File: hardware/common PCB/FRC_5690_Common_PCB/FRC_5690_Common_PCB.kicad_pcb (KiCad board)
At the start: 2 copper layers, 74.8 x 76.6 mm, 37 parts, among them J1 5V in, J10 UART, J11 LED 0, J12 LED 1, J13 Analog In, J17 Conn_01x03_Pin, J18 Conn_01x03_Pin, J19 Conn_01x03_Pin, J2 I2C, J20 Conn_01x03_Pin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

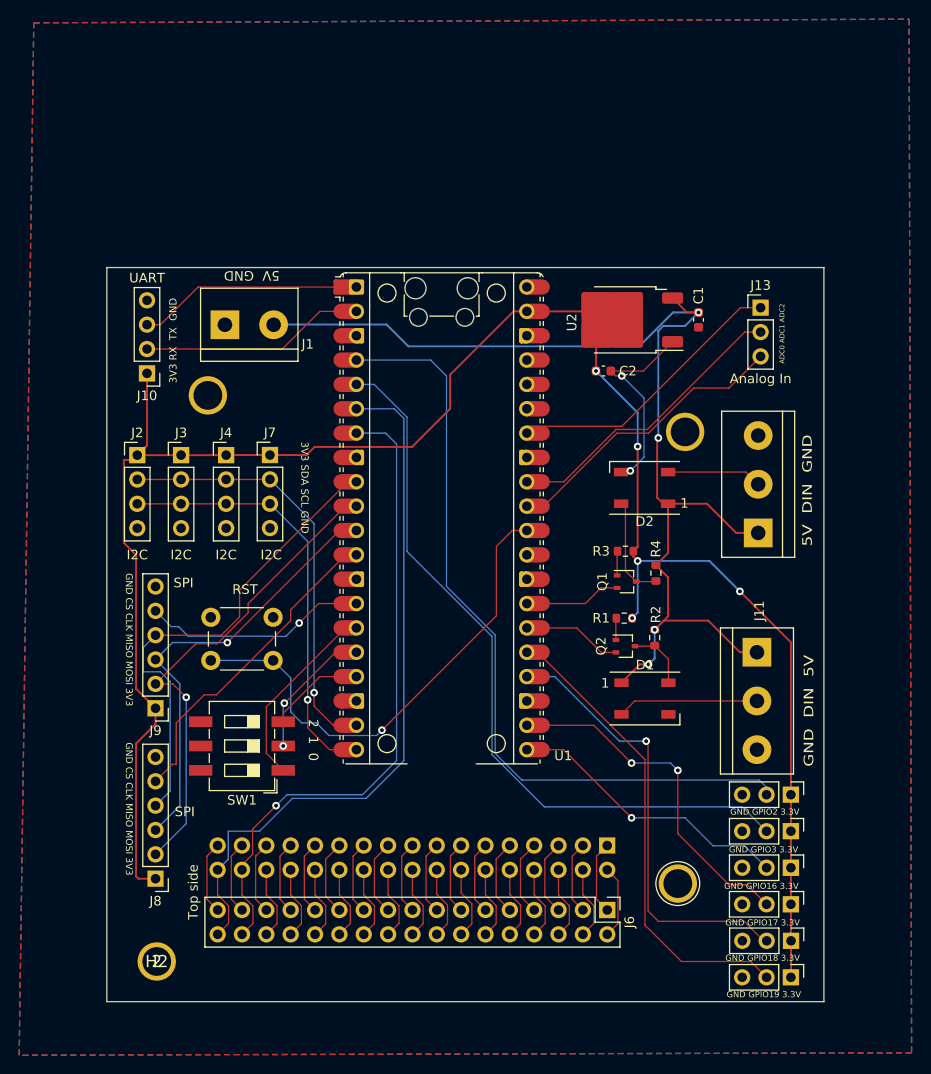
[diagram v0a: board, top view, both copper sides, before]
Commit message: migrate to Pico code and add micro SD card slot
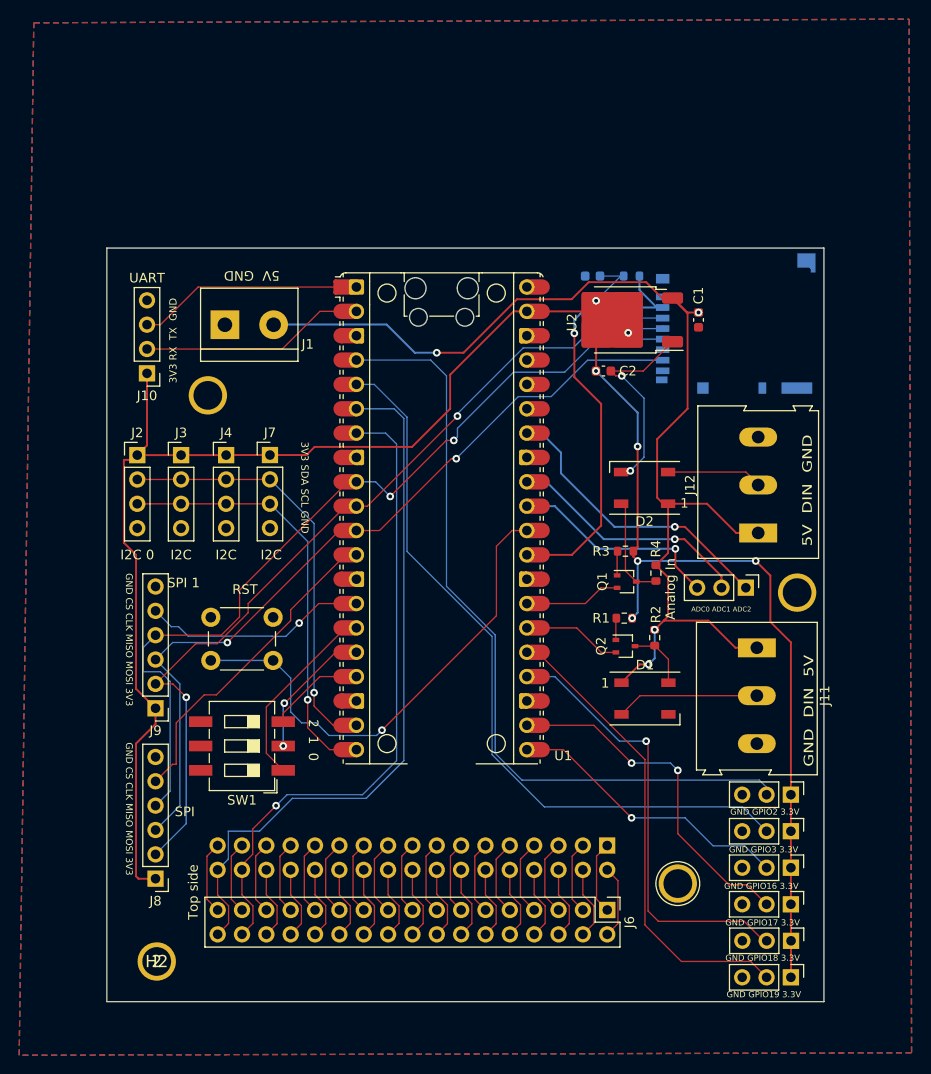
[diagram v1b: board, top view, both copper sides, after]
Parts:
- added C3: 100nF, Capacitor_SMD:C_0603_1608Metric, B.Cu at (149.9, 62.7)
- added J14: Micro_SD_Card, Connector_Card:microSD_HC_Hirose_DM3BT-DSF-PEJS, B.Cu at (164.8, 67.7)
- added R5: 1k, Resistor_SMD:R_0603_1608Metric, B.Cu at (153.9, 62.7)
- J11, J12: footprint TerminalBlock:TerminalBlock_bornier-3_P5.08mm -> TerminalBlock:TerminalBlock_Altech_AK300-3_P5.00mm
- J2: value I2C -> I2C 0
- J9: value SPI -> SPI 1
- moved J13 29.3 mm to (165.8, 95.2), turned to -90 degrees
- moved ? 20.4 mm to (171.2, 95.8)
- moved J11 0.47 mm to (167.0, 101.5)
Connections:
- U1 pad 29: unconnected-(U1-GPIO22-Pad29) -> /SD_CARD_CS
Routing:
- net /SD_CARD_CS: track 0.00 -> 46.0 mm, vias 0 -> 1
- net /SPI1_MOSI: track 50.7 -> 90.9 mm, vias 1 -> 2
- net /SPI1_CLK: track 50.4 -> 90.3 mm, vias 0 -> 2
- net /SPI1_MISO: track 46.4 -> 85.7 mm, vias 1 -> 2
- net +3.3V: track 201.2 -> 214.9 mm, vias 5 -> 7
- net /ADC0: track 30.9 -> 24.1 mm, vias 0 -> 1
- net /ADC1: track 30.9 -> 25.6 mm, vias 0 -> 1
- net /ADC2: track 29.8 -> 32.9 mm, vias 0 -> 1
- net +5V: track 117.9 -> 119.7 mm
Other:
- board size 74.8 x 76.6 mm -> 74.8 x 78.6 mm

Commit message: Add bottom silkscreen text to PCB
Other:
- board text added: "Designed by Evan Rust for FRC team 5690"
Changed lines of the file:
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@@
   (gr_rect (start 99.187 59.817) (end 173.99 138.43)
     (stroke (width 0.1) (type default)) (fill none) (layer "Edge.Cuts"))
+  (gr_text "Designed by Evan Rust for FRC team 5690" (at 151.003 117.094) (layer "B.SilkS")
+    (effects (font (size 1 1) (thickness 0.15)) (justify left bottom mirror))
+  )
   (gr_text "5V  GND" (at 117.221 62.103 180) (layer "F.SilkS")
     (effects (font (size 1 1) (thickness 0.15)) (justify left bottom))

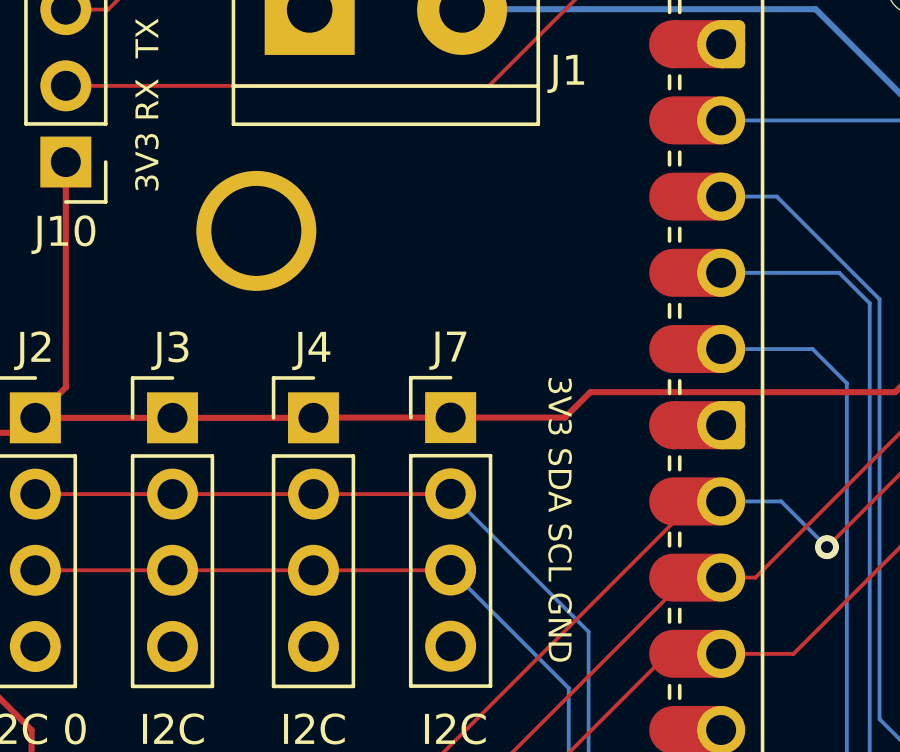
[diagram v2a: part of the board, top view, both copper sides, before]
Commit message: Add EEPROM
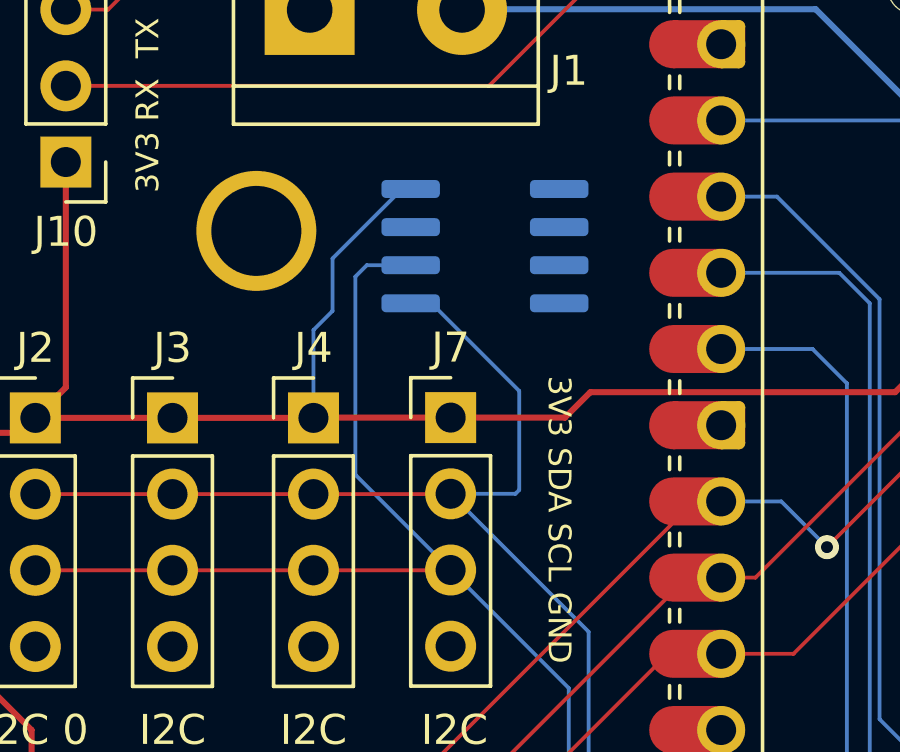
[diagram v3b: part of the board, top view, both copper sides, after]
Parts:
- added U3: AT24CS02-SSHM, Package_SO:SOIC-8_3.9x4.9mm_P1.27mm, B.Cu at (117.3, 75.7)
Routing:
- net /I2C1_SCL: track 44.9 -> 58.0 mm
- net /I2C1_SDA: track 44.6 -> 55.1 mm
- net +3.3V: track 214.9 -> 224.1 mm
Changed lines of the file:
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@@
+    )
+  )
+  (footprint "Package_SO:SOIC-8_3.9x4.9mm_P1.27mm" (layer "B.Cu")
+    (at 117.348 75.692 180)
+    (descr "SOIC, 8 Pin (JEDEC MS-012AA, https://www.analog.com/media/en/package-pcb-resources/package/pkg_pdf/soic_narrow-r/r_8.pdf), generated with kicad-footprint-generator ipc_gullwing_generator.py")
+    (tags "SOIC SO")
+    (property "Sheetfile" "FRC_5690_Common_PCB.kicad_sch")
+    (property "Sheetname" "")
+    (property "ki_description" "I2C Serial EEPROM, 2Kb (256x8) with Unique Serial Number, SO8")
+    (property "ki_keywords" "I2C Serial EEPROM Nonvolatile Memory")
+    (attr smd)
+    (fp_text reference "U3" (at 0 3.4) (layer "B.SilkS")
+        (effects (font (size 1 1) (thickness 0.15)) (justify mirror))
+    )
+    (fp_text value "AT24CS02-SSHM" (at 0 -3.4) (layer "B.Fab")
+        (effects (font (size 1 1) (thickness 0.15)) (justify mirror))
+    )
+    (fp_text user "${REFERENCE}" (at 0 0) (layer "B.Fab")
+        (effects (font (size 0.98 0.98) (thickness 0.15)) (justify mirror))
+    )
+    (fp_line (start 0 -2.56) (end -1.95 -2.56)
+      (stroke (width 0.12) (type solid)) (layer "B.SilkS"))
+    (fp_line (start 0 -2.56) (end 1.95 -2.56)
+      (stroke (width 0.12) (type solid)) (layer "B.SilkS"))
+    (fp_line (start 0 2.56) (end -3.45 2.56)
+      (stroke (width 0.12) (type solid)) (layer "B.SilkS"))
+    (fp_line (start 0 2.56) (end 1.95 2.56)
+      (stroke (width 0.12) (type solid)) (layer "B.SilkS"))
+    (fp_line (start -3.7 -2.7) (end 3.7 -2.7)
+      (stroke (width 0.05) (type solid)) (layer "B.CrtYd"))
+    (fp_line (start -3.7 2.7) (end -3.7 -2.7)
+      (stroke (width 0.05) (type solid)) (layer "B.CrtYd"))
+    (fp_line (start 3.7 -2.7) (end 3.7 2.7)
+      (stroke (width 0.05) (type solid)) (layer "B.CrtYd"))
+    (fp_line (start 3.7 2.7) (end -3.7 2.7)
+      (stroke (width 0.05) (type solid)) (layer "B.CrtYd"))
+    (fp_line (start -1.95 -2.45) (end -1.95 1.475)
+      (stroke (width 0.1) (type solid)) (layer "B.Fab"))
+    (fp_line (start -1.95 1.475) (end -0.975 2.45)
+      (stroke (width 0.1) (type solid)) (layer "B.Fab"))
+    (fp_line (start -0.975 2.45) (end 1.95 2.45)
+      (stroke (width 0.1) (type solid)) (layer "B.Fab"))
+    (fp_line (start 1.95 -2.45) (end -1.95 -2.45)
+      (stroke (width 0.1) (type solid)) (layer "B.Fab"))
+    (fp_line (start 1.95 2.45) (end 1.95 -2.45)
+      (stroke (width 0.1) (type solid)) (layer "B.Fab"))
+    (pad "1" smd roundrect (at -2.475 1.905 180) (size 1.95 0.6) (layers "B.Cu" "B.Paste" "B.Mask") (roundrect_rratio 0.25)
+      (net 7 "GND") (pinfunction "A0") (pintype "input"))
+    (pad "2" smd roundrect (at -2.475 0.635 180) (size 1.95 0.6) (layers "B.Cu" "B.Paste" "B.Mask") (roundrect_rratio 0.25)
+      (net 7 "GND") (pinfunction "A1") (pintype "input"))
+    (pad "3" smd roundrect (at -2.475 -0.635 180) (size 1.95 0.6) (layers "B.Cu" "B.Paste" "B.Mask") (roundrect_rratio 0.25)
+      (net 7 "GND") (pinfunction "A2") (pintype "input"))
+    (pad "4" smd roundrect (at -2.475 -1.905 180) (size 1.95 0.6) (layers "B.Cu" "B.Paste" "B.Mask") (roundrect_rratio 0.25)
+      (net 7 "GND") (pinfunction "GND") (pintype "power_in"))
+    (pad "5" smd roundrect (at 2.475 -1.905 180) (size 1.95 0.6) (layers "B.Cu" "B.Paste" "B.Mask") (roundrect_rratio 0.25)
+      (net 13 "/I2C1_SDA") (pinfunction "SDA") (pintype "bidirectional"))
+    (pad "6" smd roundrect (at 2.475 -0.635 180) (size 1.95 0.6) (layers "B.Cu" "B.Paste" "B.Mask") (roundrect_rratio 0.25)
+      (net 14 "/I2C1_SCL") (pinfunction "SCL") (pintype "input"))
+    (pad "7" smd roundrect (at 2.475 0.635 180) (size 1.95 0.6) (layers "B.Cu" "B.Paste" "B.Mask") (roundrect_rratio 0.25)
+      (net 7 "GND") (pinfunction "WP") (pintype "input"))
+    (pad "8" smd roundrect (at 2.475 1.905 180) (size 1.95 0.6) (layers "B.Cu" "B.Paste" "B.Mask") (roundrect_rratio 0.25)
+      (net 8 "+3.3V") (pinfunction "VCC") (pintype "power_in"))
+    (model "${KICAD6_3DMODEL_DIR}/Package_SO.3dshapes/SOIC-8_3.9x4.9mm_P1.27mm.wrl"
+      (offset (xyz 0 0 0))
+      (scale (xyz 1 1 1))
+      (rotate (xyz 0 0 0))
     )
   )
@@
   (via (at 154.559 92.456) (size 0.8) (drill 0.4) (layers "F.Cu" "B.Cu") (net 8))
   (via (at 154.559 80.518) (size 0.8) (drill 0.4) (layers "F.Cu" "B.Cu") (net 8))
+  (segment (start 114.583223 73.787) (end 112.268 76.102223) (width 0.127) (layer "B.Cu") (net 8))
+  (segment (start 114.873 73.787) (end 114.583223 73.787) (width 0.127) (layer "B.Cu") (net 8))
   (segment (start 154.559 97.853) (end 153.987 98.425) (width 0.2032) (layer "B.Cu") (net 8))
   (segment (start 150.635 62.738) (end 153.099 62.738) (width 0.127) (layer "B.Cu") (net 8))
   (segment (start 154.559 80.518) (end 154.559 76.988) (width 0.2032) (layer "B.Cu") (net 8))
+  (segment (start 112.268 76.102223) (end 112.268 77.851) (width 0.127) (layer "B.Cu") (net 8))
   (segment (start 154.559 92.456) (end 154.559 97.853) (width 0.2032) (layer "B.Cu") (net 8))
+  (segment (start 112.268 77.851) (end 111.633 78.486) (width 0.127) (layer "B.Cu") (net 8))
   (segment (start 157.169 68.219) (end 154.014 68.219) (width 0.127) (layer "B.Cu") (net 8))
+  (segment (start 111.633 78.486) (end 111.633 81.417) (width 0.127) (layer "B.Cu") (net 8))
   (segment (start 156.718 68.453) (end 157.226 67.945) (width 0.2032) (layer "B.Cu") (net 8))
   (segment (start 152.8069 62.738) (end 150.227 65.3179) (width 0.127) (layer "B.Cu") (net 8))
@@
   (segment (start 120.805 107.597) (end 120.805 106.196312) (width 0.127) (layer "F.Cu") (net 13))
   (via (at 120.805 106.196312) (size 0.8) (drill 0.4) (layers "F.Cu" "B.Cu") (net 13))
+  (segment (start 118.491 80.518) (end 118.491 83.82) (width 0.127) (layer "B.Cu") (net 13))
   (segment (start 120.805 106.196312) (end 120.805 88.547) (width 0.127) (layer "B.Cu") (net 13))
+  (segment (start 118.491 83.82) (end 118.364 83.947) (width 0.127) (layer "B.Cu") (net 13))
+  (segment (start 114.873 77.597) (end 115.57 77.597) (width 0.127) (layer "B.Cu") (net 13))
   (segment (start 120.805 88.547) (end 116.205 83.947) (width 0.127) (layer "B.Cu") (net 13))
+  (segment (start 118.364 83.947) (end 116.205 83.947) (width 0.127) (layer "B.Cu") (net 13))
+  (segment (start 115.57 77.597) (end 118.491 80.518) (width 0.127) (layer "B.Cu") (net 13))
   (segment (start 122.428 112.141) (end 125.222 112.141) (width 0.127) (layer "F.Cu") (net 14))
   (segment (start 106.934 86.497) (end 111.633 86.497) (width 0.127) (layer "F.Cu") (net 14))
@@
   (segment (start 120.142 106.934576) (end 120.142 90.424) (width 0.127) (layer "B.Cu") (net 14))
   (segment (start 120.13688 106.939696) (end 120.142 106.934576) (width 0.127) (layer "B.Cu") (net 14))
+  (segment (start 114.873 76.327) (end 113.411 76.327) (width 0.127) (layer "B.Cu") (net 14))
+  (segment (start 113.03 76.708) (end 113.03 83.312) (width 0.127) (layer "B.Cu") (net 14))
+  (segment (start 113.03 83.312) (end 116.205 86.487) (width 0.127) (layer "B.Cu") (net 14))
   (segment (start 120.142 90.424) (end 116.205 86.487) (width 0.127) (layer "B.Cu") (net 14))
+  (segment (start 113.411 76.327) (end 113.03 76.708) (width 0.127) (layer "B.Cu") (net 14))
   (segment (start 152.502499 130.293363) (end 151.388999 131.406863) (width 0.127) (layer "F.Cu") (net 15))
   (segment (start 152.502499 125.799361) (end 152.502499 130.293363) (width 0.127) (layer "F.Cu") (net 15))

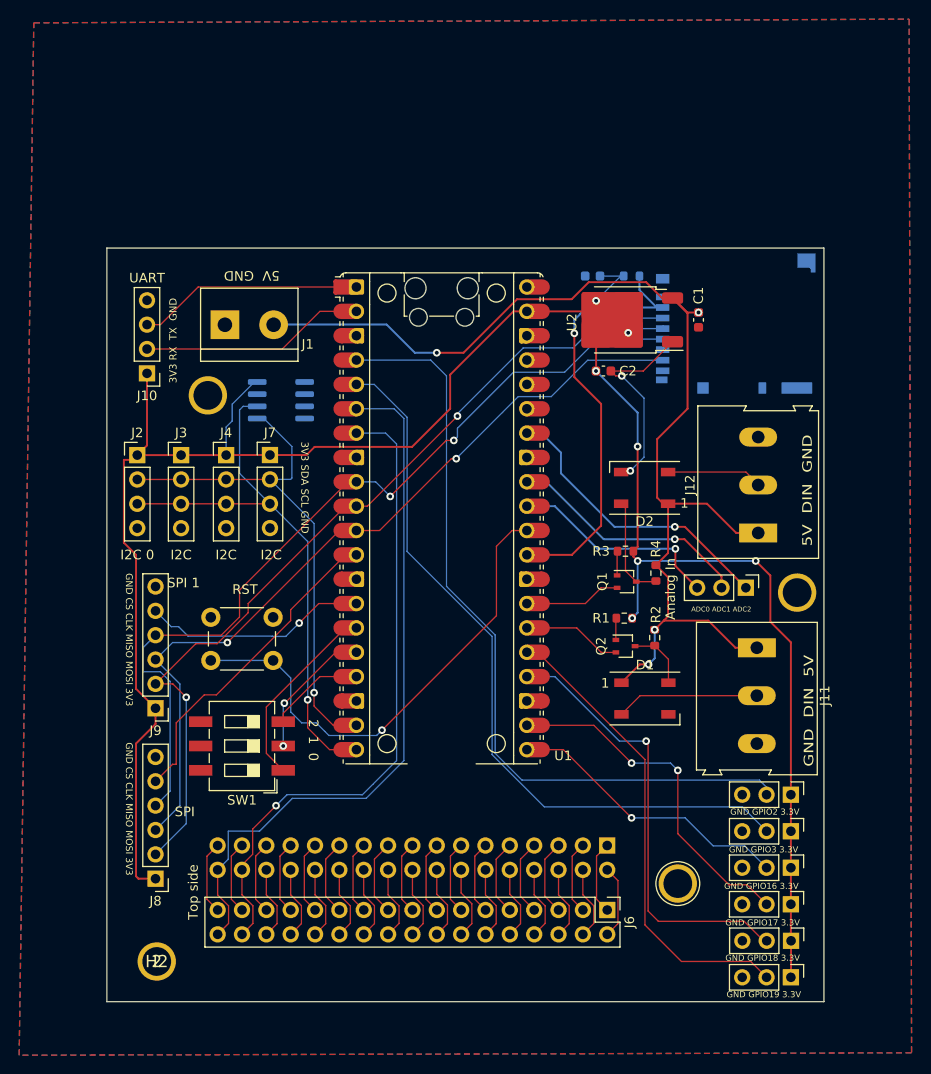
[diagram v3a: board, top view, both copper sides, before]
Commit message: add configuration for eeprom
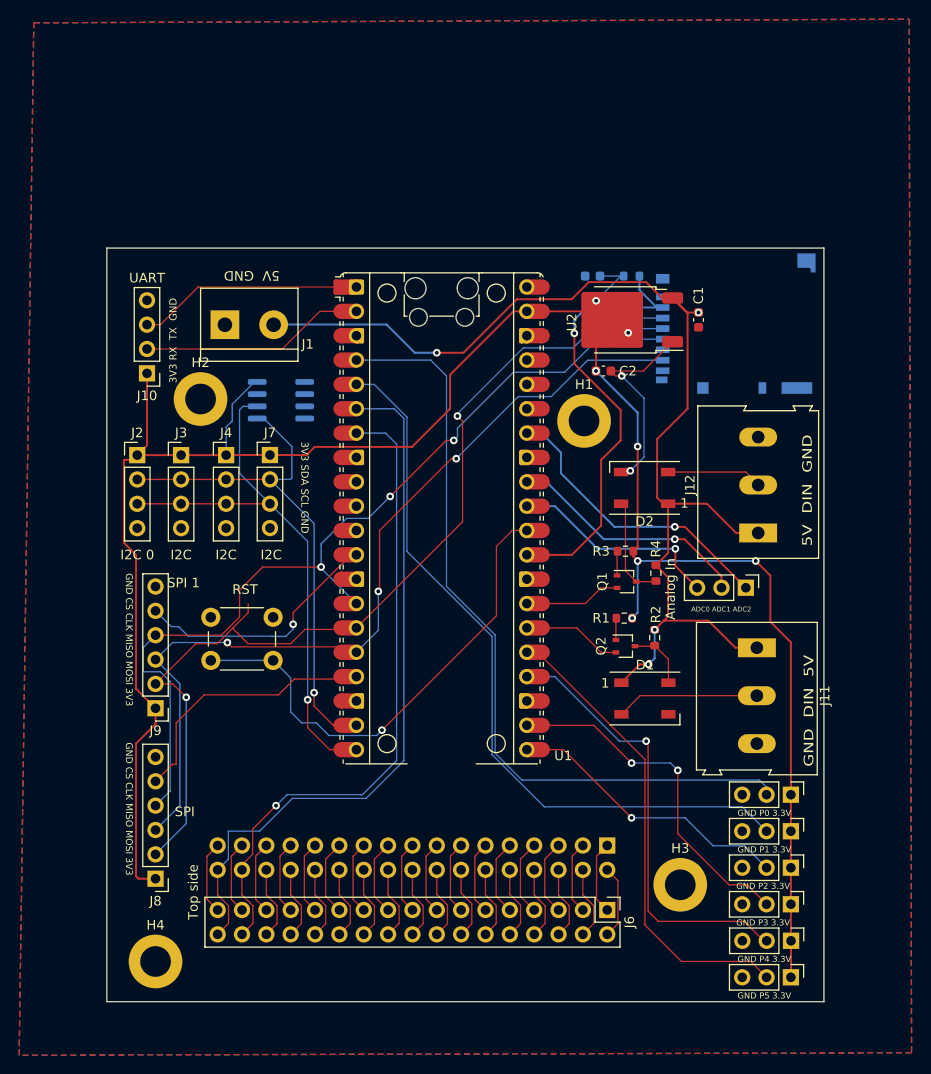
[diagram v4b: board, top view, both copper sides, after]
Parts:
- removed ? (x2): , 
- removed SW1: SW_DIP_x03, Button_Switch_SMD:SW_DIP_SPSTx03_Slide_6.7x9.18mm_W8.61mm_P2.54mm_LowProfile
- added H3: MountingHole, MountingHole:MountingHole_3.2mm_M3_DIN965_Pad, F.Cu at (159.0, 126.2)
- added H4: MountingHole, MountingHole:MountingHole_3.2mm_M3_DIN965_Pad, F.Cu at (104.3, 134.2)
- H1: value TestPoint_Plated_Hole_D3.0mm -> MountingHole; footprint TestPoint:TestPoint_Plated_Hole_D3.0mm -> MountingHole:MountingHole_3.2mm_M3_DIN965_Pad
- H2: value 2 -> MountingHole; footprint (none) -> MountingHole:MountingHole_3.2mm_M3_DIN965_Pad
- moved H2 58.9 mm to (109.0, 75.6)
- moved H1 49.2 mm to (149.0, 77.9)
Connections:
- U1 pad 10: /SPI1_MOSI -> unconnected-(U1-GPIO7-Pad10)
- U1 pad 11: /SPI1_MISO -> unconnected-(U1-GPIO8-Pad11)
- U1 pad 12: /SPI1_CS0 -> /SPI1_CS1
- U1 pad 14: /SPI1_CS1 -> /SPI1_CLK
- U1 pad 15: /ADDR_SW0 -> /SPI1_MOSI
- U1 pad 16: /ADDR_SW1 -> /SPI1_MISO
- U1 pad 17: /ADDR_SW2 -> /SPI1_CS0
- U1 pad 9: /SPI1_CLK -> unconnected-(U1-GPIO6-Pad9)
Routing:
- net /ADDR_SW0: track 20.2 -> 0.00 mm
- net /ADDR_SW1: track 14.3 -> 0.00 mm, vias 2 -> 0
- net /SPI1_MOSI: track 90.9 -> 103.3 mm
- net /ADDR_SW2: track 10.1 -> 0.00 mm
- net /SPI1_MISO: track 85.7 -> 94.7 mm, vias 2 -> 3
- net /SPI1_CS0: track 33.9 -> 28.0 mm
- net /SPI1_CLK: track 90.3 -> 95.7 mm, vias 2 -> 3
- net /SPI1_CS1: track 23.5 -> 27.7 mm
- net unconnected-(U1-GPIO8-Pad11): track 0.00 -> 1.77 mm
- net /SD_CARD_CS: track 46.0 -> 47.7 mm
- net unconnected-(U1-GPIO7-Pad10): track 0.00 -> 1.13 mm
- net unconnected-(U1-GPIO6-Pad9): track 0.00 -> 0.89 mm
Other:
- board text added: "GND P0 3.3V"
- board text added: "GND P1 3.3V"
- board text added: "GND P2 3.3V"
- board text added: "GND P3 3.3V"
- board text added: "GND P4 3.3V"
- board text added: "GND P5 3.3V"
- board text removed: "2 1 0"
- board text removed: "GND GPIO16 3.3V"
- board text removed: "GND GPIO17 3.3V"
- board text removed: "GND GPIO18 3.3V"
- board text removed: "GND GPIO19 3.3V"
- board text removed: "GND GPIO2 3.3V"
- board text removed: "GND GPIO3 3.3V"
